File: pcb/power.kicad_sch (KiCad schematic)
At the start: 10 parts, among them U2 nPM1300-QEXX

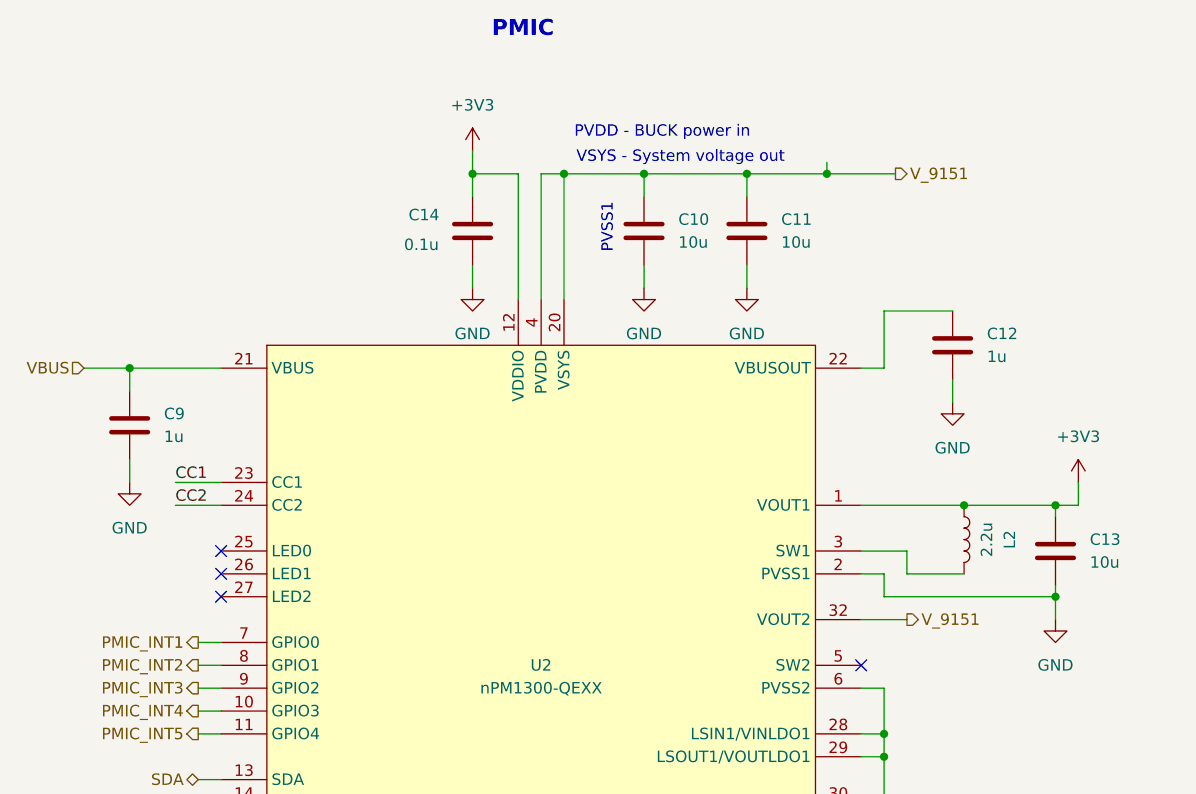
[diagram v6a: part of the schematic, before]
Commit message: Fix display sch
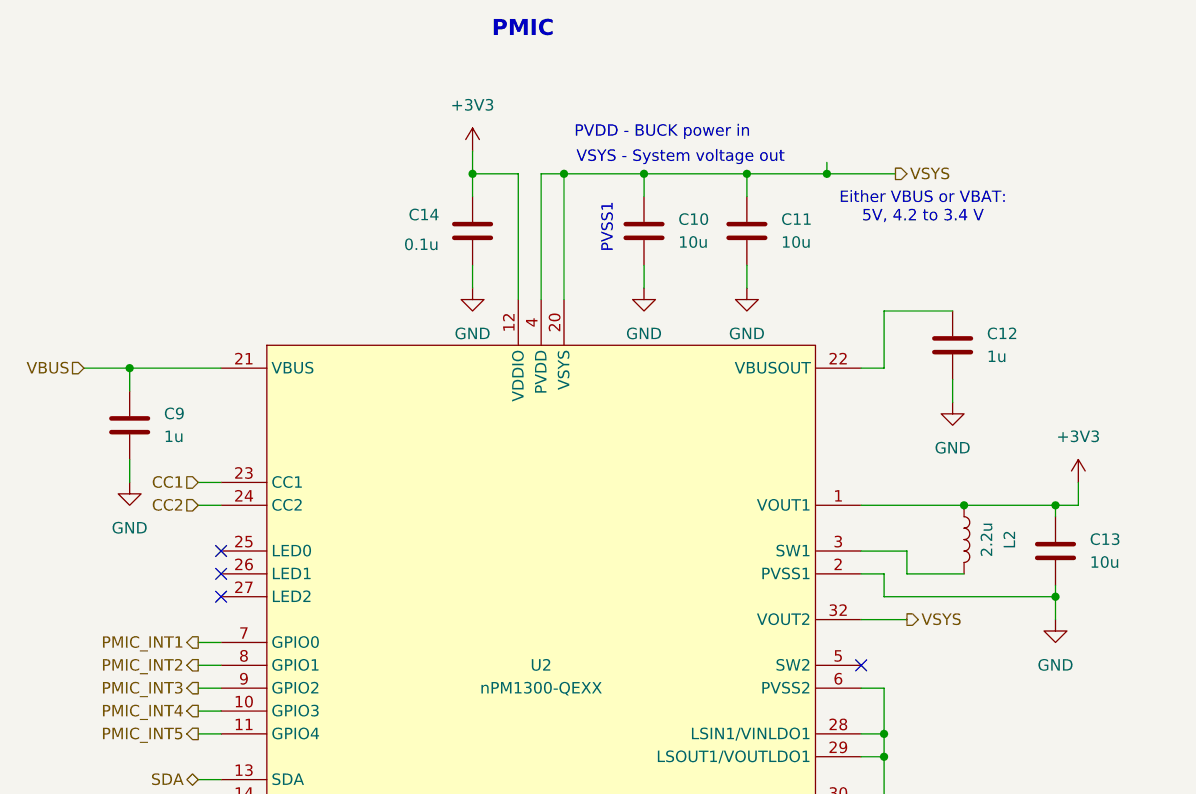
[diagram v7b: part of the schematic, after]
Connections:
- net V_9151 renamed VSYS
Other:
- note added: "Either VBUS or VBAT: 5V, 4.2 to 3.4 V"
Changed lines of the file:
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@@
+		)
+	)
+	(text "Either VBUS or VBAT:\n5V, 4.2 to 3.4 V"
+		(exclude_from_sim no)
+		(at 196.088 54.61 0)
+		(effects
+			(font
+				(size 1.27 1.27)
+			)
 		)
 	)
@@
 	(wire
 		(pts
+			(xy 115.57 85.09) (xy 118.11 85.09)
+		)
+		(stroke
+			(width 0)
+			(type default)
+		)
+	)
+	(wire
+		(pts
 			(xy 191.77 120.65) (xy 191.77 123.19)
 		)
@@
 	(wire
 		(pts
-			(xy 113.03 85.09) (xy 118.11 85.09)
-		)
-		(stroke
-			(width 0)
-			(type default)
-		)
-	)
-	(wire
-		(pts
 			(xy 191.77 97.79) (xy 191.77 95.25)
 		)
@@
 	(wire
 		(pts
-			(xy 113.03 87.63) (xy 118.11 87.63)
-		)
-		(stroke
-			(width 0)
-			(type default)
-		)
-	)
-	(wire
-		(pts
 			(xy 115.57 102.87) (xy 118.11 102.87)
 		)
@@
 	(wire
 		(pts
+			(xy 115.57 87.63) (xy 118.11 87.63)
+		)
+		(stroke
+			(width 0)
+			(type default)
+		)
+	)
+	(wire
+		(pts
 			(xy 189.23 107.95) (xy 191.77 107.95)
 		)
@@
 			(width 0)
 			(type default)
-		)
-	)
-	(label "CC1"
-		(at 113.03 85.09 0)
-		(effects
-			(font
-				(size 1.27 1.27)
-			)
-			(justify left bottom)
-		)
-	)
-	(label "CC2"
-		(at 113.03 87.63 0)
-		(effects
-			(font
-				(size 1.27 1.27)
-			)
-			(justify left bottom)
 		)
 	)
@@
 		)
 	)
-	(hierarchical_label "V_9151"
+	(hierarchical_label "VSYS"
 		(shape output)
 		(at 193.04 50.8 0)
@@
 		)
 	)
+	(hierarchical_label "CC2"
+		(shape input)
+		(at 115.57 87.63 180)
+		(effects
+			(font
+				(size 1.27 1.27)
+			)
+			(justify right)
+		)
+	)
 	(hierarchical_label "PMIC_INT5"
 		(shape output)
@@
 		)
 	)
+	(hierarchical_label "CC1"
+		(shape input)
+		(at 115.57 85.09 180)
+		(effects
+			(font
+				(size 1.27 1.27)
+			)
+			(justify right)
+		)
+	)
 	(hierarchical_label "VBAT"
 		(shape input)
@@
 		)
 	)
-	(hierarchical_label "V_9151"
+	(hierarchical_label "VSYS"
 		(shape output)
 		(at 194.31 100.33 0)
